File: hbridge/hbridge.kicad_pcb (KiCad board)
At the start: 2 copper layers, 211.5 x 106.7 mm, 22 parts, among them J1 From_MCU, J10 From_MCU, J11 MOSFET_out, J12 Conn_01x03, J13 Conn_01x01_Socket, J14 Conn_01x01_Socket, J19 24V, J2 MOSFET_out, J3 Conn_01x03, J4 From_MCU, J5 MOSFET_out, J6 Conn_01x03, J7 From_MCU, J8 MOSFET_out, J9 Conn_01x03, U1 LDO-3.3, U20 B2412S-2WR3, U4 AM6TW-2415DZ, U9 AM6TW-2415DZ

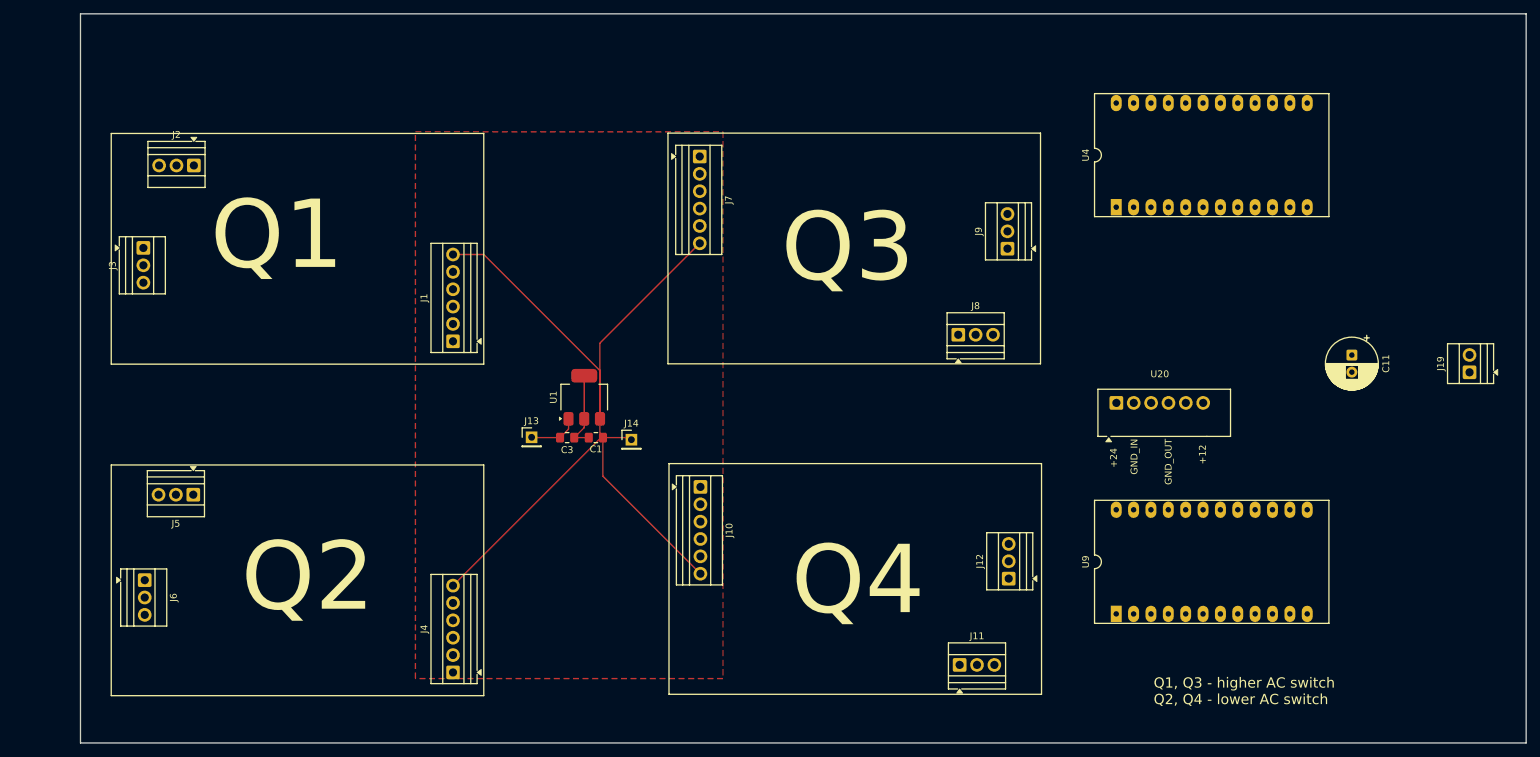
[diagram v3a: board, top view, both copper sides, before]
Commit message: Half-bridge, no MCU.
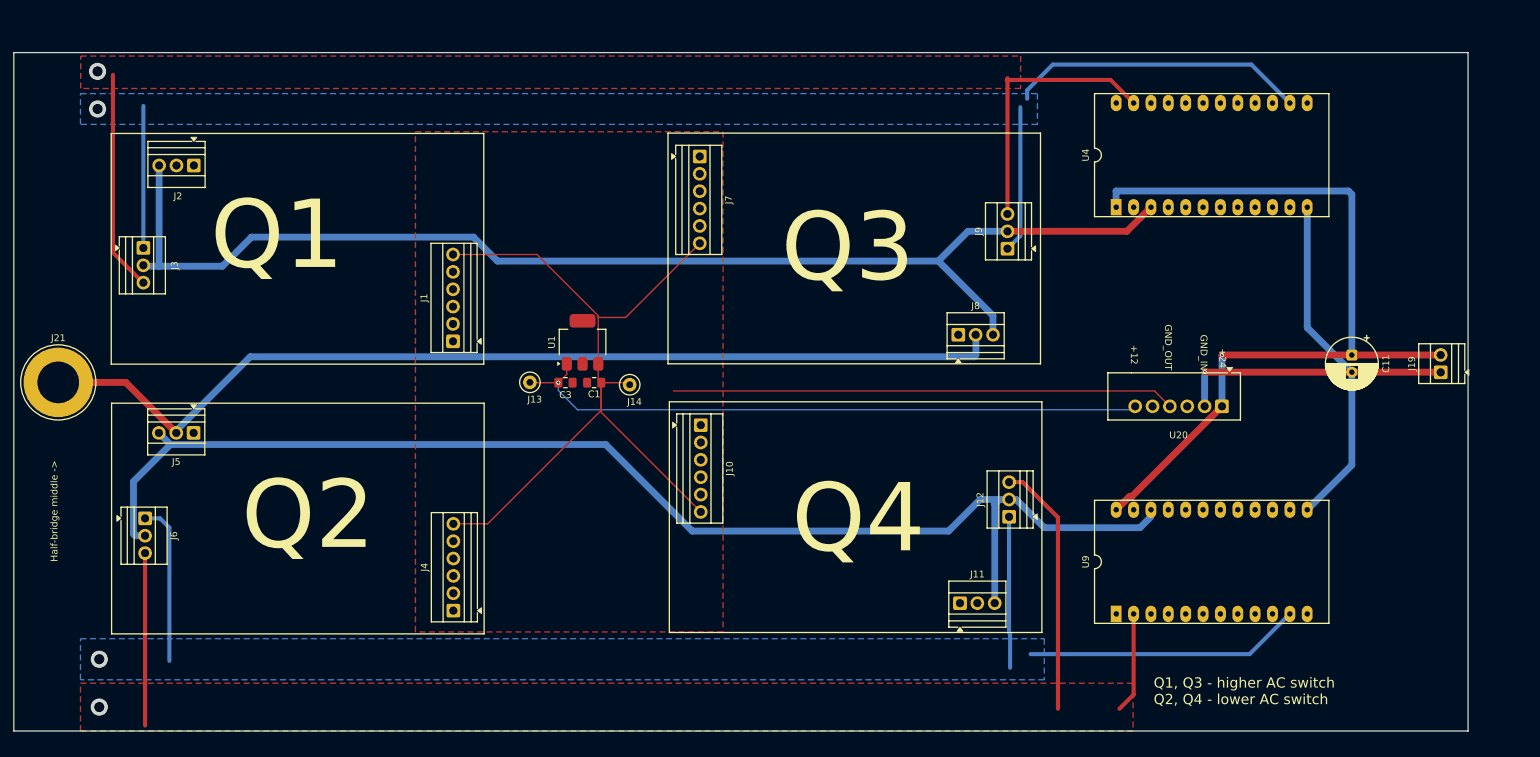
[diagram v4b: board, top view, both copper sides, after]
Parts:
- added J21: Conn_01x01_Socket, Connector:Banana_Jack_1Pin, F.Cu at (36.8, 91.2)
- J13, J14: footprint Connector_PinHeader_2.54mm:PinHeader_1x01_P2.54mm_Vertical -> TestPoint:TestPoint_Loop_D1.80mm_Drill1.0mm_Beaded
- moved U20 15.5 mm to (207.0, 94.8), turned to 180 degrees
- moved J10 9.04 mm to (130.8, 97.5)
- moved J11 9.04 mm to (168.7, 123.5)
- moved J4 9.04 mm to (94.5, 124.6)
- moved J5 9.04 mm to (56.5, 98.6)
- moved J6 9.04 mm to (49.5, 111.1)
- moved J12 9.04 mm to (175.8, 110.9)
- moved C1 8.05 mm to (115.2, 91.3)
- moved C3 8.05 mm to (111.0, 91.3)
- moved J13 8.05 mm to (105.8, 91.2)
- moved J14 8.05 mm to (120.3, 91.6)
- moved U1 8.05 mm to (113.5, 85.4)
- moved J19 4.22 mm to (239.0, 89.8)
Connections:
- J8 pad 2: /драйверы/drain3 -> /драйверы/drain2
- U20 pad 4: Net-(U20-GND_OUT) -> GND_DRV1
- U4 pad 22: GND_DRV2_H -> unconnected-(U4-COM-Pad22)
- U4 pad 3: unconnected-(U4-COM-Pad3) -> GND_DRV2_H
- U9 pad 1: +24V_1 -> unconnected-(U9-+VIN-Pad1)
- U9 pad 10: GND_DRV2_L -> unconnected-(U9-COM-Pad10)
- U9 pad 12: GND1 -> unconnected-(U9--VIN-Pad12)
- U9 pad 14: +15_DRV2_L -> unconnected-(U9-+VOUT-Pad14)
- U9 pad 15: GND_DRV2_L -> unconnected-(U9-COM-Pad15)
- U9 pad 23: -15_DRV2_L -> unconnected-(U9--VOUT-Pad23)
- U9 pad 3: GND_DRV2_L -> unconnected-(U9-COM-Pad3)
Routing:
- net GND_DRV2_L: track 0.00 -> 190.4 mm
- net GND_DRV2_H: track 0.00 -> 182.8 mm
- net /драйверы/drain2: track 0.00 -> 145.2 mm
- net +24V_1: track 0.00 -> 121.3 mm, vias 0 -> 1
- net GND1: track 0.00 -> 89.1 mm, vias 0 -> 1
- net +12V: track 7.45 -> 94.4 mm, vias 0 -> 1
- net +15_DRV2_L: track 0.00 -> 86.1 mm, vias 0 -> 1
- net +15_DRV2_H: track 0.00 -> 85.8 mm, vias 0 -> 1
- net -15_DRV2_L: track 0.00 -> 77.3 mm, vias 0 -> 1
- net -15_DRV2_H: track 0.00 -> 72.1 mm, vias 0 -> 1
- net GND_DRV1: track 11.8 -> 73.6 mm
- net +3V3_DRV1: track 131.2 -> 116.3 mm
- added copper zone on B.Cu, net +15_DRV2_H
- added copper zone on B.Cu, net +15_DRV2_L
- added copper zone on F.Cu, net -15_DRV2_H
- added copper zone on F.Cu, net -15_DRV2_L
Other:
- board size 211.5 x 106.7 mm -> 212.8 x 99.2 mm
- board text added: "Half-bridge middle ->"

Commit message: Hierarchy changed. MCU optocouplers started.
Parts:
- added J20: Conn_01x04, Connector_PinHeader_2.54mm:PinHeader_1x04_P2.54mm_Vertical, F.Cu at (57.0, 38.2)
- added J22: Conn_01x04, Connector_PinHeader_2.54mm:PinHeader_1x04_P2.54mm_Vertical, F.Cu at (81.2, 29.0)
- added J23: Conn_01x04, Connector_PinHeader_2.54mm:PinHeader_1x04_P2.54mm_Vertical, F.Cu at (130.6, 34.2)
- added J24: Conn_01x04, Connector_PinHeader_2.54mm:PinHeader_1x04_P2.54mm_Vertical, F.Cu at (157.8, 31.0)
- added U5: Optocoupler_4chan, Package_SO:SOIC-16W_7.5x10.3mm_P1.27mm, F.Cu at (155.7, 164.3)
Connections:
- J1 pad 2: /драйверы/IN1 -> IN1
- J1 pad 3: /драйверы/RDY1 -> RDY1
- J1 pad 4: /драйверы/FLT1 -> FLT1
- J1 pad 5: /драйверы/EN1 -> EN1
- J10 pad 2: /драйверы/IN4 -> IN4
- J10 pad 3: /драйверы/RDY4 -> RDY4
- J10 pad 4: /драйверы/FLT4 -> FLT4
- J10 pad 5: /драйверы/EN4 -> EN4
- J4 pad 2: /драйверы/IN2 -> IN2
- J4 pad 3: /драйверы/RDY2 -> RDY2
- J4 pad 4: /драйверы/FLT2 -> FLT2
- J4 pad 5: /драйверы/EN2 -> EN2
- J7 pad 2: /драйверы/IN3 -> IN3
- J7 pad 3: /драйверы/RDY3 -> RDY3
- J7 pad 4: /драйверы/FLT3 -> FLT3
- J7 pad 5: /драйверы/EN3 -> EN3

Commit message: Optocoupler schema changed.
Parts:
- moved U5 7.16 mm to (149.5, 160.8)

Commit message: Driver board: castellated holes. SMD diode.
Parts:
- added R13: 1k, Resistor_SMD:R_0402_1005Metric_Pad0.72x0.64mm_HandSolder, F.Cu at (134.1, 98.2)
- added R14: 1k, Resistor_SMD:R_0805_2012Metric_Pad1.20x1.40mm_HandSolder, F.Cu at (147.7, 86.7)
- added R15: 1k, Resistor_SMD:R_0402_1005Metric_Pad0.72x0.64mm_HandSolder, F.Cu at (134.1, 100.2)
- added R16: 1k, Resistor_SMD:R_0805_2012Metric_Pad1.20x1.40mm_HandSolder, F.Cu at (147.7, 89.7)
- added R17: 1k, Resistor_SMD:R_0402_1005Metric_Pad0.72x0.64mm_HandSolder, F.Cu at (134.1, 102.2)
- added R18: 1k, Resistor_SMD:R_0402_1005Metric_Pad0.72x0.64mm_HandSolder, F.Cu at (134.1, 104.2)
- added R19: 1k, Resistor_SMD:R_0805_2012Metric_Pad1.20x1.40mm_HandSolder, F.Cu at (147.7, 92.6)
- added R20: 1k, Resistor_SMD:R_0805_2012Metric_Pad1.20x1.40mm_HandSolder, F.Cu at (147.7, 95.6)
- J20, J22: value Conn_01x04 -> Conn_01x06; footprint Connector_PinHeader_2.54mm:PinHeader_1x04_P2.54mm_Vertical -> Connector_PinHeader_2.54mm:PinHeader_1x06_P2.54mm_Vertical
- moved J20 140.4 mm to (156.0, 137.8)
- moved J4 130.6 mm to (180.3, 223.1)
- moved J5 130.6 mm to (142.3, 197.1)
- moved C1 130.6 mm to (200.9, 189.8)
- moved C11 130.6 mm to (311.8, 185.7)
- moved C3 130.6 mm to (196.7, 189.8)
- moved J1 130.6 mm to (180.2, 183.7)
- moved J10 130.6 mm to (216.5, 196.0)
- moved J12 130.6 mm to (261.6, 209.4)
- moved J13 130.6 mm to (191.5, 189.7)
- moved J14 130.6 mm to (206.1, 190.1)
- moved J19 130.6 mm to (324.8, 188.2)
- moved J21 130.6 mm to (122.5, 189.7)
- moved J23 130.6 mm to (216.4, 132.7)
- moved J24 130.6 mm to (243.5, 129.5)
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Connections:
- J20 pad 1: EN1 -> +12V_opt
- J20 pad 2: FLT1 -> EN1_opto
- J20 pad 3: RDY1 -> FLT1_opto
- J20 pad 4: IN1 -> RDY1_opto
- J22 pad 1: EN2 -> +12V_opt
- J22 pad 2: FLT2 -> EN1_opto
- J22 pad 3: RDY2 -> FLT1_opto
- J22 pad 4: IN2 -> RDY1_opto
- U5 pad 1: unconnected-(U5-Pad1) -> Net-(R14-Pad1)
- U5 pad 10: unconnected-(U5-Pad10) -> +3V3
- U5 pad 11: unconnected-(U5-Pad11) -> RDY1_opto
- U5 pad 12: unconnected-(U5-Pad12) -> +12V_opt
- U5 pad 13: unconnected-(U5-Pad13) -> FLT1_opto
- U5 pad 14: unconnected-(U5-Pad14) -> +12V_opt
- U5 pad 15: unconnected-(U5-Pad15) -> EN1
- U5 pad 16: unconnected-(U5-Pad16) -> +3V3
- U5 pad 2: unconnected-(U5-Pad2) -> GND_opt
- U5 pad 3: unconnected-(U5-Pad3) -> Net-(R19-Pad2)
- U5 pad 4: unconnected-(U5-Pad4) -> GND_DRV1_H
- U5 pad 5: unconnected-(U5-Pad5) -> Net-(R20-Pad2)
- U5 pad 6: unconnected-(U5-Pad6) -> GND_DRV1_H
- U5 pad 7: unconnected-(U5-Pad7) -> Net-(R16-Pad1)
- U5 pad 8: unconnected-(U5-Pad8) -> GND_opt
- U5 pad 9: unconnected-(U5-Pad9) -> IN1
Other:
- board size 212.8 x 99.2 mm -> 212.8 x 164.2 mm

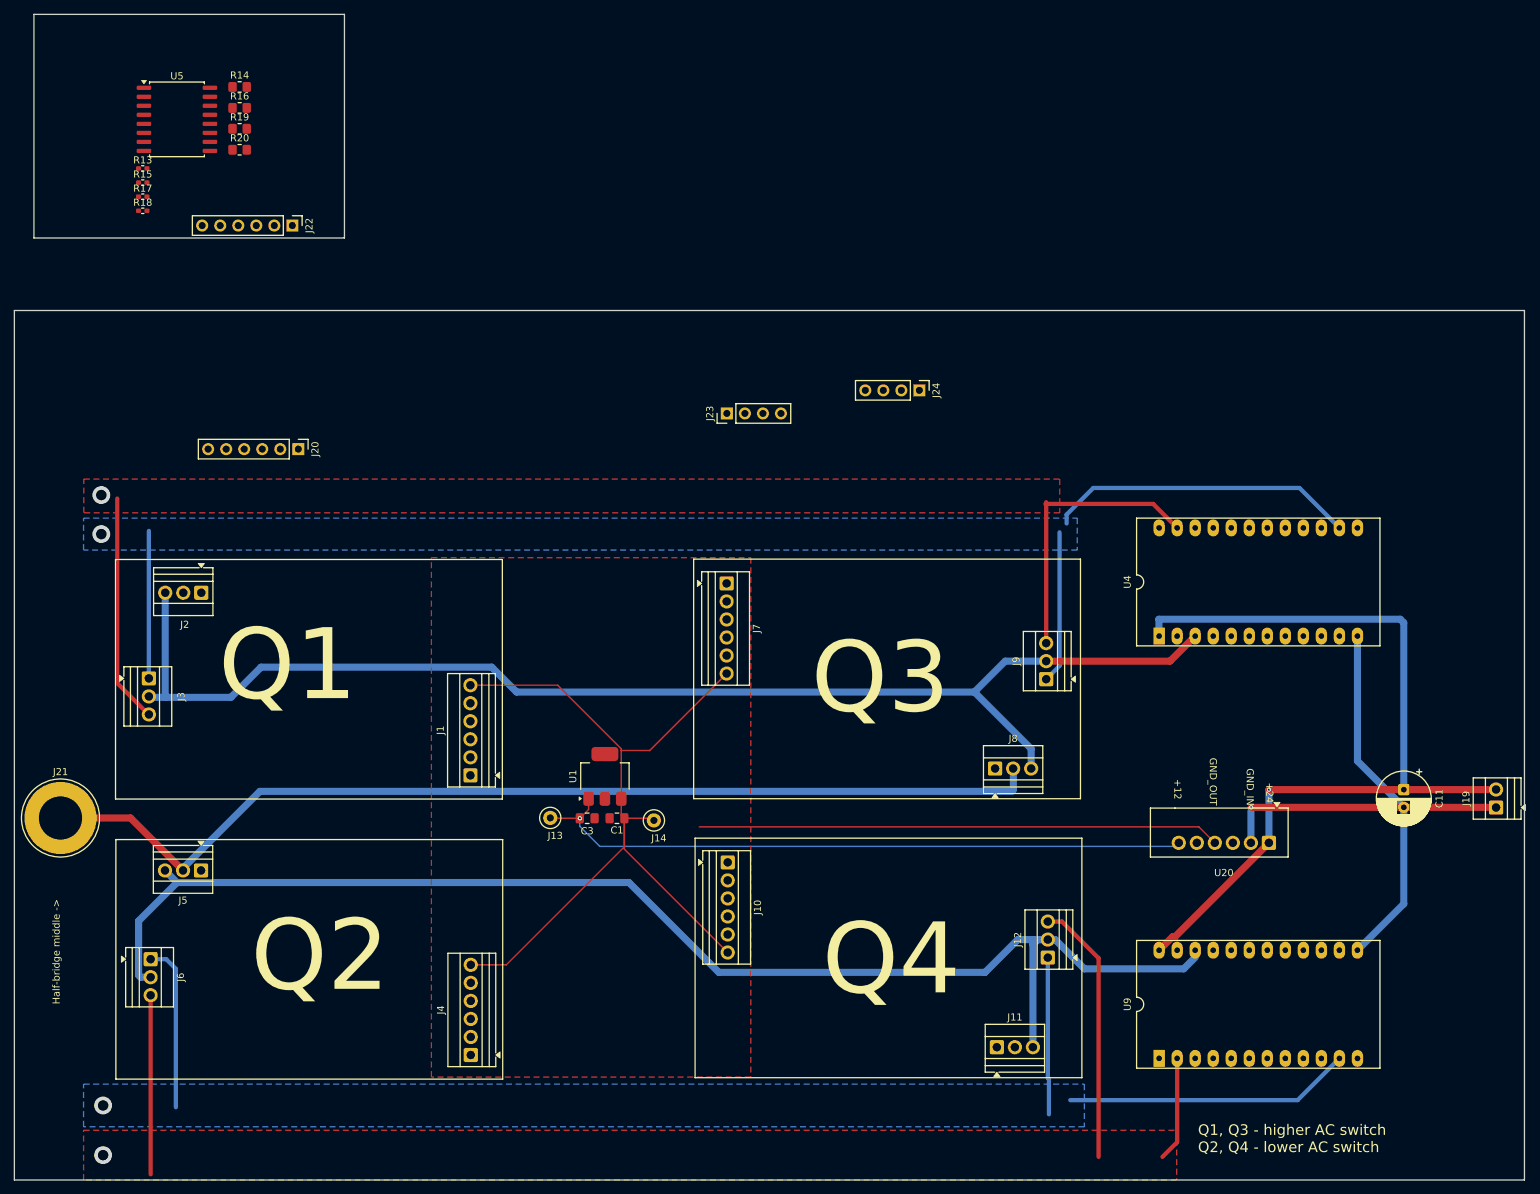
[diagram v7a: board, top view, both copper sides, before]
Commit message: Half-bridge board: driver defence circuit added.
Logical circuit on AND, NOT, RS-latch, Shift-register.
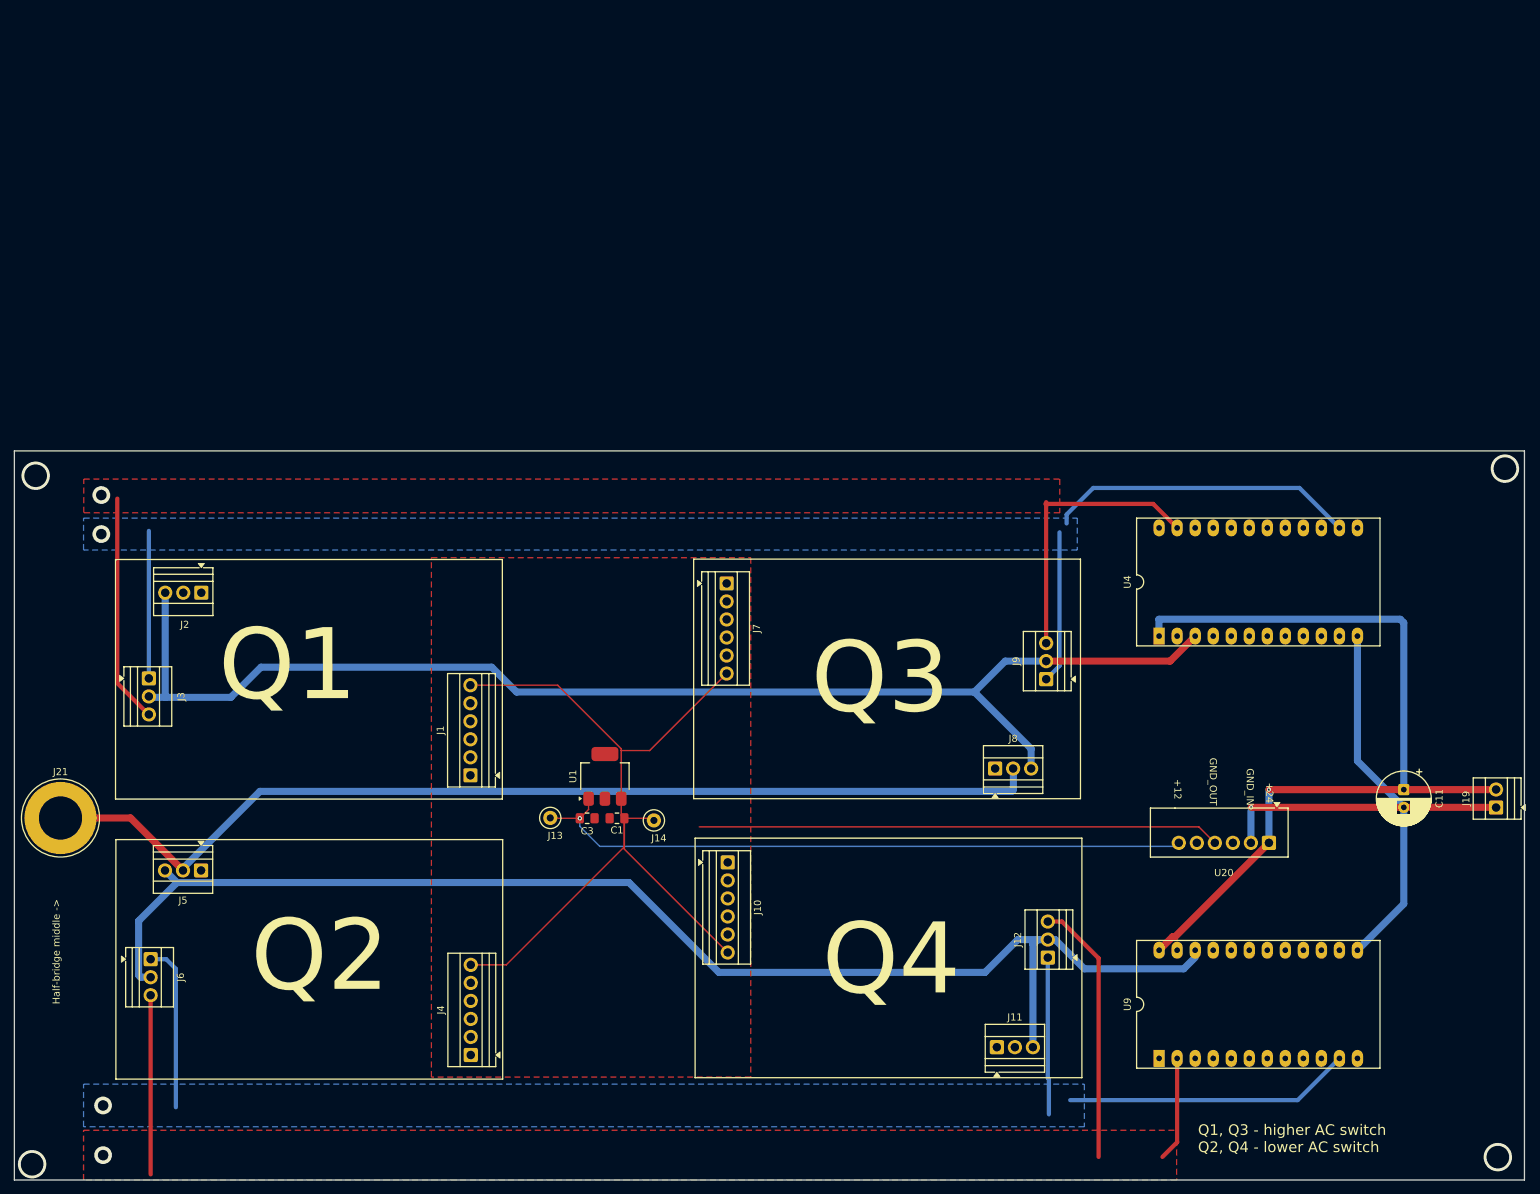
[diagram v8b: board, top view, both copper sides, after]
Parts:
- removed J20, J22: Conn_01x06, Connector_PinHeader_2.54mm:PinHeader_1x06_P2.54mm_Vertical
- removed J23, J24: Conn_01x04, Connector_PinHeader_2.54mm:PinHeader_1x04_P2.54mm_Vertical
- removed R13, R15, R17, R18: 1k, Resistor_SMD:R_0402_1005Metric_Pad0.72x0.64mm_HandSolder
- removed R14, R16, R19, R20: 1k, Resistor_SMD:R_0805_2012Metric_Pad1.20x1.40mm_HandSolder
- removed U5: Optocoupler_4chan, Package_SO:SOIC-16W_7.5x10.3mm_P1.27mm
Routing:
- net (no net): vias 0 -> 4
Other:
- board size 212.8 x 164.2 mm -> 212.8 x 102.7 mm
